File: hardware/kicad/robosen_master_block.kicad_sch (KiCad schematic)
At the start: 13 parts, among them J1 CONFIG_DOCK_PORT, J2 RUN_CHAIN_PORT, SW1 Knob 1 (Action), SW2 Knob 2 (Param), SW3 START_BUTTON, SW4 POWER_SWITCH, U1 ESP32-S3-DevKitC-1, U2 TP4056_USB-C_BMS, U3 TPS63020_3.3V_BuckBoost

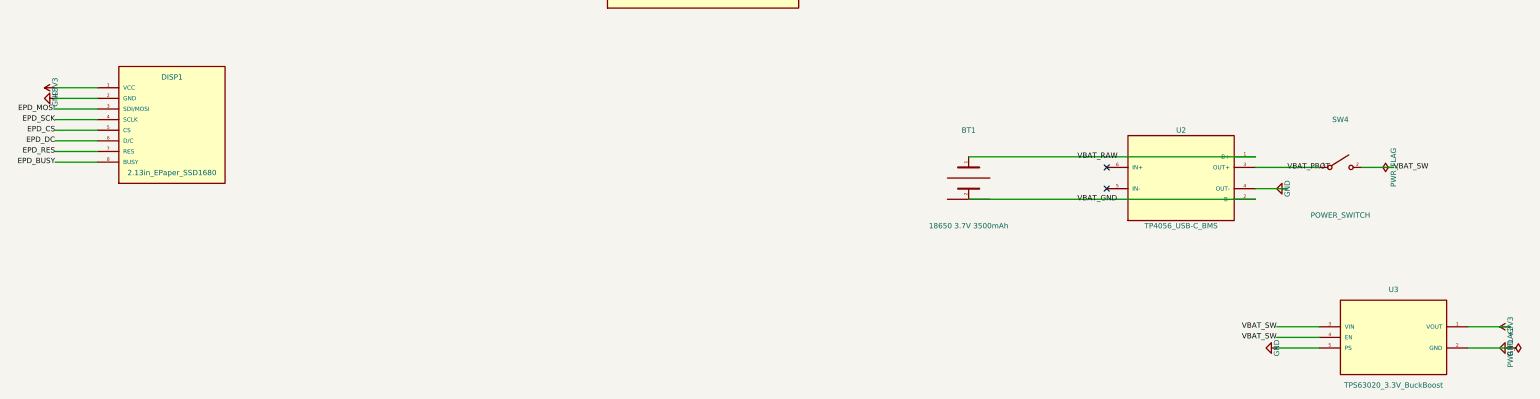
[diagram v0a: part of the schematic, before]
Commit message: hardware(kicad): align footprints with physical measurements and update docs
- ESP32-S3 DevKitC-1: orient socket (Antenna Top, USB-C Bottom) with Left 1-22 and Right 23-44 pinout
- E-Paper 2.13in: update pinout to 1:BUSY, 2:CS, 3:DC, 4:RES, 5:SDA, 6:SCL, 7:VCC, 8:GND
- TPS63020 Buck-Boost: match manufacturer drawing (26.32x17.51mm, 23.78mm span, 2.54mm corner pitch)
- TP4056 USB-C: update to horizontal layout (25.6x17mm, 21.7mm span, right column OUT+/B+/B-/OUT-)
- build_schematic: re-route power wiring cleanly, verify KiCad ERC (0 violations)
- Update hardware/kicad/README.md and root README.md documentation
- Include initial robosen_master_block.kicad_pcb board file
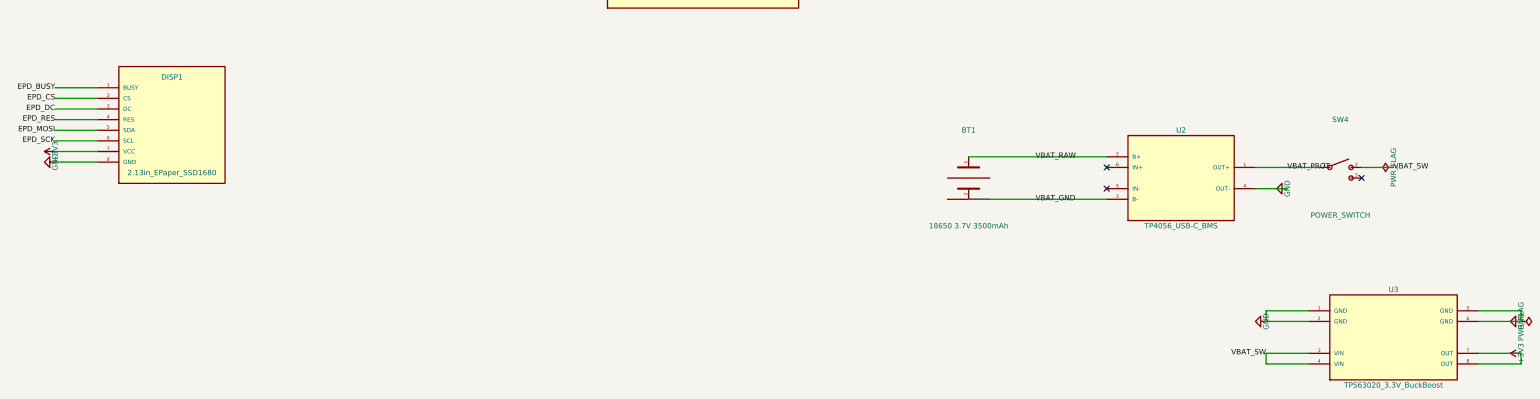
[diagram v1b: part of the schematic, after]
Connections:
- net +3V3: now also DISP1.7 (VCC), U3.7 (OUT), U3.8 (OUT); no longer DISP1.1 (VCC), U3.1 (VOUT)
- net EPD_BUSY: now also DISP1.1 (BUSY); no longer DISP1.8 (BUSY)
- net EPD_CS: now also DISP1.2 (CS); no longer DISP1.5 (CS)
- net EPD_DC: now also DISP1.3 (DC); no longer DISP1.6 (D/C)
- net EPD_MOSI: now also DISP1.5 (SDA); no longer DISP1.3 (SDI/MOSI)
- net EPD_RES: now also DISP1.4 (RES); no longer DISP1.7 (RES)
- net EPD_SCK: now also DISP1.6 (SCL); no longer DISP1.4 (SCLK)
- net GND: now also DISP1.8 (GND), U3.1 (GND), U3.6 (GND); no longer DISP1.2 (GND)
- net VBAT_GND: now also U2.3 (B-); no longer U2.2 (B-)
- net VBAT_PROT: now also U2.1 (OUT+); no longer U2.3 (OUT+)
- net VBAT_RAW: now also U2.2 (B+); no longer U2.1 (B+)
- no-connect marks 23 -> 24

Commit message: hardware(kicad): finalize physical footprints for KY-040, 2-wire switch, and 18650 holder
- KY-040 Rotary Encoder: 25x18mm footprint with vertical 5-pin header (2.54mm pitch), dual 3.2mm mounting holes, and knob shaft outline
- Power Switch: create SW_Power_2Wire_Pads with 5.08mm (1-hole gap) pitch for easy wire soldering and heatshrink clearance
- 18650 Battery Holder: 77.5x20.5mm with dual 3.2mm mounting holes (55.5mm span) and external wire solder pads (Left +, Right -)
- Schematic & Symbols: update SW_SPST to 2-pin switch, remove pin 3 no_conn, verify KiCad ERC (0 violations)
- Update hardware/kicad/README.md documentation with complete verification matrix
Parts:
- SW4: footprint robosen_master:SW_Slide_SS12D00 -> robosen_master:SW_Power_2Wire_Pads
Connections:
- no-connect marks 24 -> 23
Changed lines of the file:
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@@
 		(instances
 			(project "robosen_master_block"
-				(path "/fca7690e-e71b-4732-8b4c-4f2b0a5a0fc6"
+				(path "/ffc97304-7a46-4344-aeb8-9b80b62f18ec"
 					(reference "U1")
 					(unit 1)
@@
 		(instances
 			(project "robosen_master_block"
-				(path "/fca7690e-e71b-4732-8b4c-4f2b0a5a0fc6"
+				(path "/ffc97304-7a46-4344-aeb8-9b80b62f18ec"
 					(reference "SW1")
 					(unit 1)
@@
 		(instances
 			(project "robosen_master_block"
-				(path "/fca7690e-e71b-4732-8b4c-4f2b0a5a0fc6"
+				(path "/ffc97304-7a46-4344-aeb8-9b80b62f18ec"
 					(reference "SW2")
 					(unit 1)
@@
 		(instances
 			(project "robosen_master_block"
-				(path "/fca7690e-e71b-4732-8b4c-4f2b0a5a0fc6"
+				(path "/ffc97304-7a46-4344-aeb8-9b80b62f18ec"
 					(reference "SW3")
 					(unit 1)
@@
 		(instances
 			(project "robosen_master_block"
-				(path "/fca7690e-e71b-4732-8b4c-4f2b0a5a0fc6"
+				(path "/ffc97304-7a46-4344-aeb8-9b80b62f18ec"
 					(reference "DISP1")
 					(unit 1)
@@
 		(instances
 			(project "robosen_master_block"
-				(path "/fca7690e-e71b-4732-8b4c-4f2b0a5a0fc6"
+				(path "/ffc97304-7a46-4344-aeb8-9b80b62f18ec"
 					(reference "J1")
 					(unit 1)
@@
 		(instances
 			(project "robosen_master_block"
-				(path "/fca7690e-e71b-4732-8b4c-4f2b0a5a0fc6"
+				(path "/ffc97304-7a46-4344-aeb8-9b80b62f18ec"
 					(reference "J2")
 					(unit 1)
@@
 		(instances
 			(project "robosen_master_block"
-				(path "/fca7690e-e71b-4732-8b4c-4f2b0a5a0fc6"
+				(path "/ffc97304-7a46-4344-aeb8-9b80b62f18ec"
 					(reference "R1")
 					(unit 1)
@@
 		(instances
 			(project "robosen_master_block"
-				(path "/fca7690e-e71b-4732-8b4c-4f2b0a5a0fc6"
+				(path "/ffc97304-7a46-4344-aeb8-9b80b62f18ec"
 					(reference "R2")
 					(unit 1)
@@
 		(instances
 			(project "robosen_master_block"
-				(path "/fca7690e-e71b-4732-8b4c-4f2b0a5a0fc6"
+				(path "/ffc97304-7a46-4344-aeb8-9b80b62f18ec"
 					(reference "BT1")
 					(unit 1)
@@
 		(instances
 			(project "robosen_master_block"
-				(path "/fca7690e-e71b-4732-8b4c-4f2b0a5a0fc6"
+				(path "/ffc97304-7a46-4344-aeb8-9b80b62f18ec"
 					(reference "U2")
 					(unit 1)
@@
 		(property "Reference" "SW4" (at 342.90 201.93 0) (effects (font (size 1.27 1.27))))
 		(property "Value" "POWER_SWITCH" (at 342.90 224.79 0) (effects (font (size 1.27 1.27))))
-		(property "Footprint" "robosen_master:SW_Slide_SS12D00" (at 342.90 213.36 0) (effects (font (size 1.27 1.27)) (hide yes)))
+		(property "Footprint" "robosen_master:SW_Power_2Wire_Pads" (at 342.90 213.36 0) (effects (font (size 1.27 1.27)) (hide yes)))
 		(property "Datasheet" "" (at 342.90 213.36 0) (effects (font (size 1.27 1.27)) (hide yes)))
 		(property "Description" "" (at 342.90 213.36 0) (effects (font (size 1.27 1.27)) (hide yes)))
 		(pin "1")
 		(pin "2")
-		(pin "3")
-		(instances
-			(project "robosen_master_block"
-				(path "/fca7690e-e71b-4732-8b4c-4f2b0a5a0fc6"
+		(instances
+			(project "robosen_master_block"
+				(path "/ffc97304-7a46-4344-aeb8-9b80b62f18ec"
 					(reference "SW4")
 					(unit 1)
@@
 		(instances
 			(project "robosen_master_block"
-				(path "/fca7690e-e71b-4732-8b4c-4f2b0a5a0fc6"
+				(path "/ffc97304-7a46-4344-aeb8-9b80b62f18ec"
 					(reference "U3")
 					(unit 1)
@@
 		(instances
 			(project "robosen_master_block"
-				(path "/fca7690e-e71b-4732-8b4c-4f2b0a5a0fc6"
+				(path "/ffc97304-7a46-4344-aeb8-9b80b62f18ec"
 					(reference "#PWR01")
 					(unit 1)
@@
 		(instances
 			(project "robosen_master_block"
-				(path "/fca7690e-e71b-4732-8b4c-4f2b0a5a0fc6"
+				(path "/ffc97304-7a46-4344-aeb8-9b80b62f18ec"
 					(reference "#PWR02")
 					(unit 1)
@@
 		(instances
 			(project "robosen_master_block"
-				(path "/fca7690e-e71b-4732-8b4c-4f2b0a5a0fc6"
+				(path "/ffc97304-7a46-4344-aeb8-9b80b62f18ec"
 					(reference "#PWR03")
 					(unit 1)
@@
 		(instances
 			(project "robosen_master_block"
-				(path "/fca7690e-e71b-4732-8b4c-4f2b0a5a0fc6"
+				(path "/ffc97304-7a46-4344-aeb8-9b80b62f18ec"
 					(reference "#PWR04")
 					(unit 1)
@@
 		(instances
 			(project "robosen_master_block"
-				(path "/fca7690e-e71b-4732-8b4c-4f2b0a5a0fc6"
+				(path "/ffc97304-7a46-4344-aeb8-9b80b62f18ec"
 					(reference "#PWR05")
 					(unit 1)
@@
 		(instances
 			(project "robosen_master_block"
-				(path "/fca7690e-e71b-4732-8b4c-4f2b0a5a0fc6"
+				(path "/ffc97304-7a46-4344-aeb8-9b80b62f18ec"
 					(reference "#PWR06")
 					(unit 1)
@@
 		(instances
 			(project "robosen_master_block"
-				(path "/fca7690e-e71b-4732-8b4c-4f2b0a5a0fc6"
+				(path "/ffc97304-7a46-4344-aeb8-9b80b62f18ec"
 					(reference "#PWR07")
 					(unit 1)
@@
 		(instances
 			(project "robosen_master_block"
-				(path "/fca7690e-e71b-4732-8b4c-4f2b0a5a0fc6"
+				(path "/ffc97304-7a46-4344-aeb8-9b80b62f18ec"
 					(reference "#PWR08")
 					(unit 1)
@@
 		(instances
 			(project "robosen_master_block"
-				(path "/fca7690e-e71b-4732-8b4c-4f2b0a5a0fc6"
+				(path "/ffc97304-7a46-4344-aeb8-9b80b62f18ec"
 					(reference "#PWR09")
 					(unit 1)
@@
 		(instances
 			(project "robosen_master_block"
-				(path "/fca7690e-e71b-4732-8b4c-4f2b0a5a0fc6"
+				(path "/ffc97304-7a46-4344-aeb8-9b80b62f18ec"
 					(reference "#PWR10")
 					(unit 1)
@@
 		(instances
 			(project "robosen_master_block"
-				(path "/fca7690e-e71b-4732-8b4c-4f2b0a5a0fc6"
+				(path "/ffc97304-7a46-4344-aeb8-9b80b62f18ec"
 					(reference "#PWR11")
 					(unit 1)
@@
 		(instances
 			(project "robosen_master_block"
-				(path "/fca7690e-e71b-4732-8b4c-4f2b0a5a0fc6"
+				(path "/ffc97304-7a46-4344-aeb8-9b80b62f18ec"
 					(reference "#PWR12")
 					(unit 1)
@@
 		(instances
 			(project "robosen_master_block"
-				(path "/fca7690e-e71b-4732-8b4c-4f2b0a5a0fc6"
+				(path "/ffc97304-7a46-4344-aeb8-9b80b62f18ec"
 					(reference "#PWR13")
 					(unit 1)
@@
 		(instances
 			(project "robosen_master_block"
-				(path "/fca7690e-e71b-4732-8b4c-4f2b0a5a0fc6"
+				(path "/ffc97304-7a46-4344-aeb8-9b80b62f18ec"
 					(reference "#PWR14")
 					(unit 1)
@@
 		(instances
 			(project "robosen_master_block"
-				(path "/fca7690e-e71b-4732-8b4c-4f2b0a5a0fc6"
+				(path "/ffc97304-7a46-4344-aeb8-9b80b62f18ec"
 					(reference "#PWR15")
 					(unit 1)
@@
 		(instances
 			(project "robosen_master_block"
-				(path "/fca7690e-e71b-4732-8b4c-4f2b0a5a0fc6"
+				(path "/ffc97304-7a46-4344-aeb8-9b80b62f18ec"
 					(reference "#PWR16")
 					(unit 1)
@@
 		(instances
 			(project "robosen_master_block"
-				(path "/fca7690e-e71b-4732-8b4c-4f2b0a5a0fc6"
+				(path "/ffc97304-7a46-4344-aeb8-9b80b62f18ec"
 					(reference "#PWR17")
 					(unit 1)
@@
 		(instances
 			(project "robosen_master_block"
-				(path "/fca7690e-e71b-4732-8b4c-4f2b0a5a0fc6"
+				(path "/ffc97304-7a46-4344-aeb8-9b80b62f18ec"
 					(reference "#PWR18")
 					(unit 1)
@@
 		(instances
 			(project "robosen_master_block"
-				(path "/fca7690e-e71b-4732-8b4c-4f2b0a5a0fc6"
+				(path "/ffc97304-7a46-4344-aeb8-9b80b62f18ec"
 					(reference "#PWR19")
 					(unit 1)
@@
 		(instances
 			(project "robosen_master_block"
-				(path "/fca7690e-e71b-4732-8b4c-4f2b0a5a0fc6"
+				(path "/ffc97304-7a46-4344-aeb8-9b80b62f18ec"
 					(reference "#PWR20")
 					(unit 1)
@@
 		(instances
 			(project "robosen_master_block"
-				(path "/fca7690e-e71b-4732-8b4c-4f2b0a5a0fc6"
+				(path "/ffc97304-7a46-4344-aeb8-9b80b62f18ec"
 					(reference "#FLG02")
 					(unit 1)
@@
 		)
 	)
-	(no_connect (at 347.98 215.90))
 	(wire (pts (xy 335.28 247.65) (xy 325.12 247.65)) (stroke (width 0) (type solid)))
 	(wire (pts (xy 335.28 250.19) (xy 325.12 250.19)) (stroke (width 0) (type solid)))
@@
 		(instances
 			(project "robosen_master_block"
-				(path "/fca7690e-e71b-4732-8b4c-4f2b0a5a0fc6"
+				(path "/ffc97304-7a46-4344-aeb8-9b80b62f18ec"
 					(reference "#PWR21")
 					(unit 1)
@@
 		(instances
 			(project "robosen_master_block"
-				(path "/fca7690e-e71b-4732-8b4c-4f2b0a5a0fc6"
+				(path "/ffc97304-7a46-4344-aeb8-9b80b62f18ec"
 					(reference "#PWR23")
 					(unit 1)
@@
 		(instances
 			(project "robosen_master_block"
-				(path "/fca7690e-e71b-4732-8b4c-4f2b0a5a0fc6"
+				(path "/ffc97304-7a46-4344-aeb8-9b80b62f18ec"
 					(reference "#FLG01")
 					(unit 1)
@@
 		(instances
 			(project "robosen_master_block"
-				(path "/fca7690e-e71b-4732-8b4c-4f2b0a5a0fc6"
+				(path "/ffc97304-7a46-4344-aeb8-9b80b62f18ec"
 					(reference "#PWR22")
 					(unit 1)

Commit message: feat(hardware): implement battery percentage monitoring divider and ADC filter (Task 1)
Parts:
- added C1: 100nF (ADC Filter), robosen_master:C_Disc_P2.54mm, symbol robosen_master:C
- added R3, R4: 100k (1% Batt Div), robosen_master:R_Axial_P10.16mm, symbol robosen_master:R
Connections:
- net GND: now also C1.1, R4.2
- net VBAT_SW: now also R3.1
- net BATSENSE: now reaches U1.26 (GPIO1)
- net BATSENSE: now also C1.2, R3.2, R4.1
- no-connect marks 23 -> 22

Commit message: feat(hardware): implement dual-button UI (green confirm / red cancel) in schematic and PCB (Task 5)
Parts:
- added SW5: CANCEL_STOP (Red), robosen_master:SW_PUSH_12x12mm, symbol robosen_master:SW_Push
- SW3: value START_BUTTON -> CONFIRM_START (Green)
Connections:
- net GND: now also SW5.2
- net BTN_STOP: now reaches U1.27 (GPIO2)
- net BTN_STOP: now also SW5.1
- no-connect marks 22 -> 21
